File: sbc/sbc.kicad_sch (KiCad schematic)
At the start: 15 parts, among them U1 Sally, U2 Antic, U3 GTIA, U4 Pokey, U5 PIA, U6 74AHCT1G125GV,125, U7 74AHCT1G125GV,125, X1 3.579545 MHz

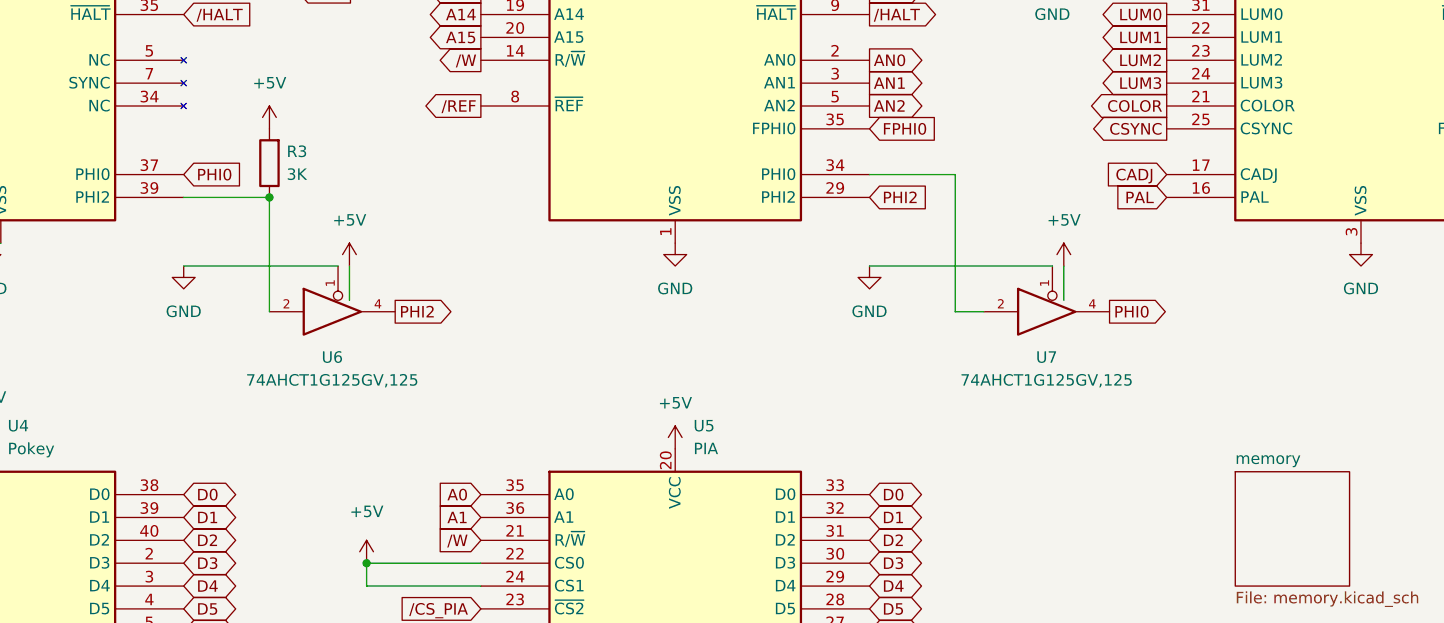
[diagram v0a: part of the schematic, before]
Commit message: SBC v1.1
PCB fixes/changes:

  - Permanently power voltage translators
  - Conservatively specified a slower SRAM (the previous/faster SRAM does actually work fine)
  - RMU: Speculatively provided unbuffered PHI0 input and OE output (not actually needed)
  - Add pullups to open drain GTIA outputs
  - Plot selected values on silk screen
  - Accommodate KiCad 7 upgrade

- PLD changes:
  - Fix AMU logic
  - Fix RMU (unbuffered PHI0 and OE output not needed)

- QTPY firmware:
  - add soft power on/off support (Ctrl-F12)
  - reflects switched power and usb state in the neopixel
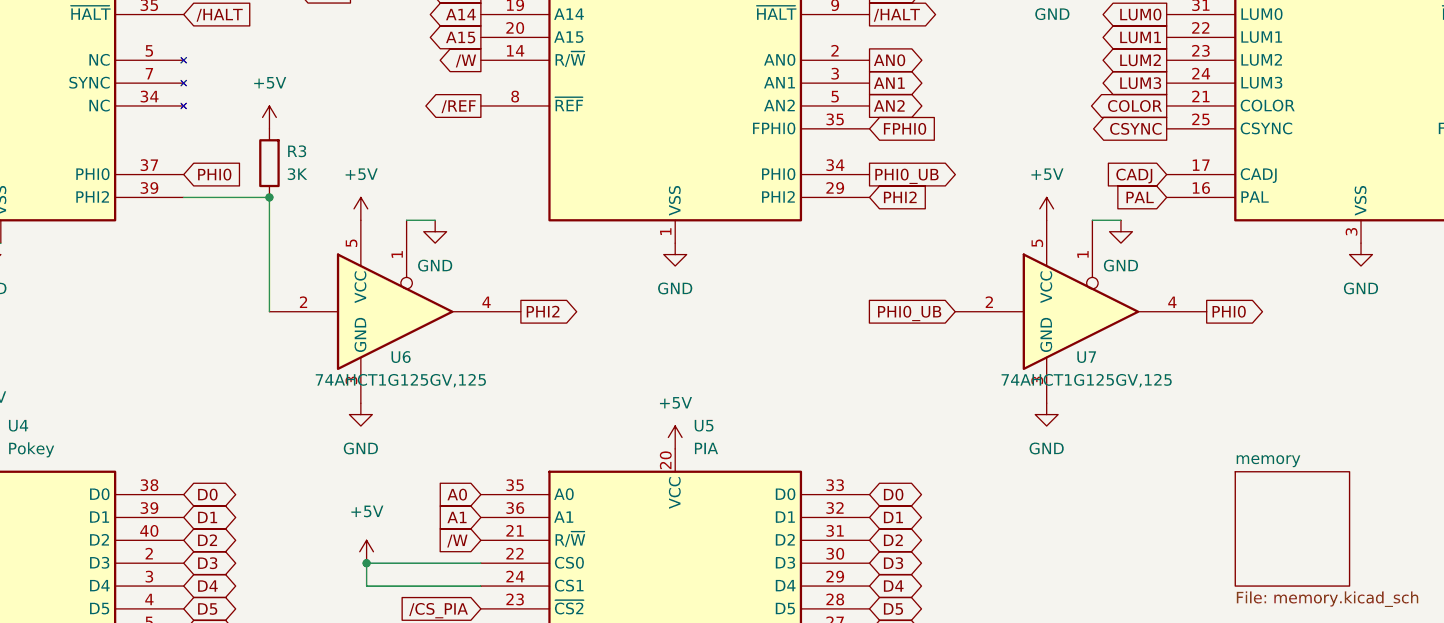
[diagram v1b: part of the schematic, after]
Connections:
- net PHI0_UB: now reaches U2.34 (PHI0), U7.2

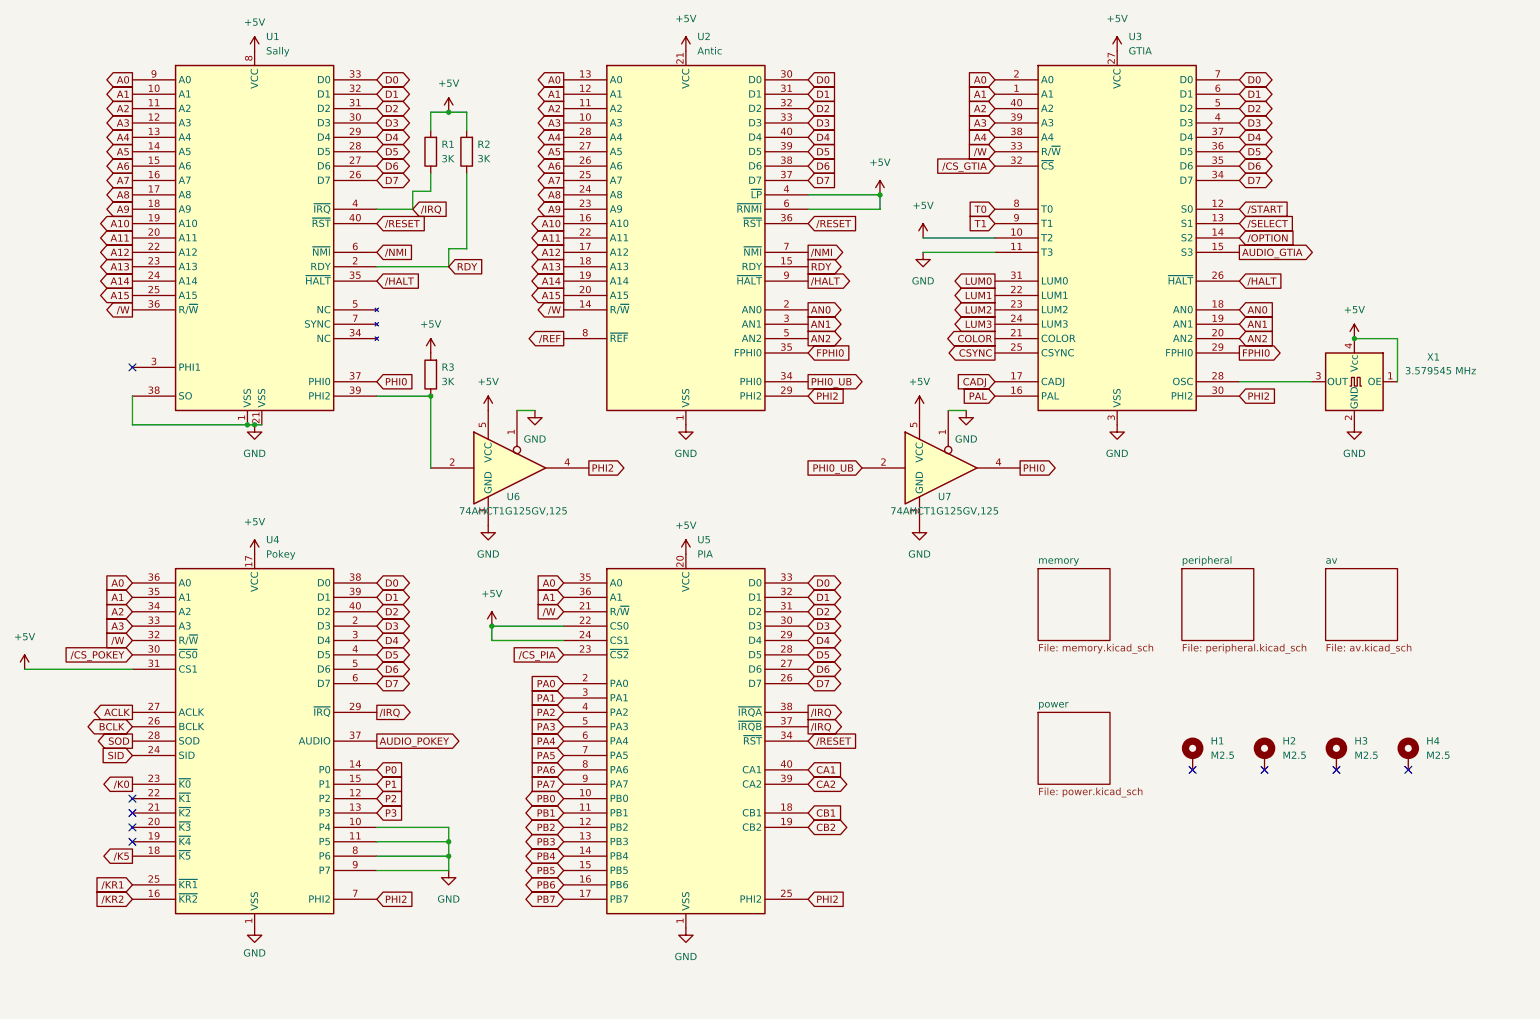
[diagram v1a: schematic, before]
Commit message: SBC v1.2
SBC fixes/changes:

  - S-Video:
    - Fix S-Video footprint (Y and C swapped, and GNDs swapped) and adapt schematic to match
    - Wire S-Video grounds to AVA header instead of directly to (digital) GND
  - Audio:
    - Wire Audio-Out ground to AVA header
    - Drop SIO audio
    - Pullup open drain pokey audio
  - AMU/RMU:
    - Connect ROM and RAM OE to GND
    - Reserve AMU pin for "IO"
    - Reserve RMU pin for "antic" (registered halt)
    - Support for separate Antic banking (clock RMU with /phi2)
    - Supoprt 130XE and 320XE (compy)
  - Add the option for a resistor between OSC, PHI0 buffer and PHI2 buffer (to reduce over/under-shoot)
  - Invert CA2 (a PNP transistor on the Atari 800 XL inverts this signal)

Additions:

  - SBC Audio/Video board
  - SBC Case
  - SBC SD board

Stylize the complete system as "SFF 320XE".
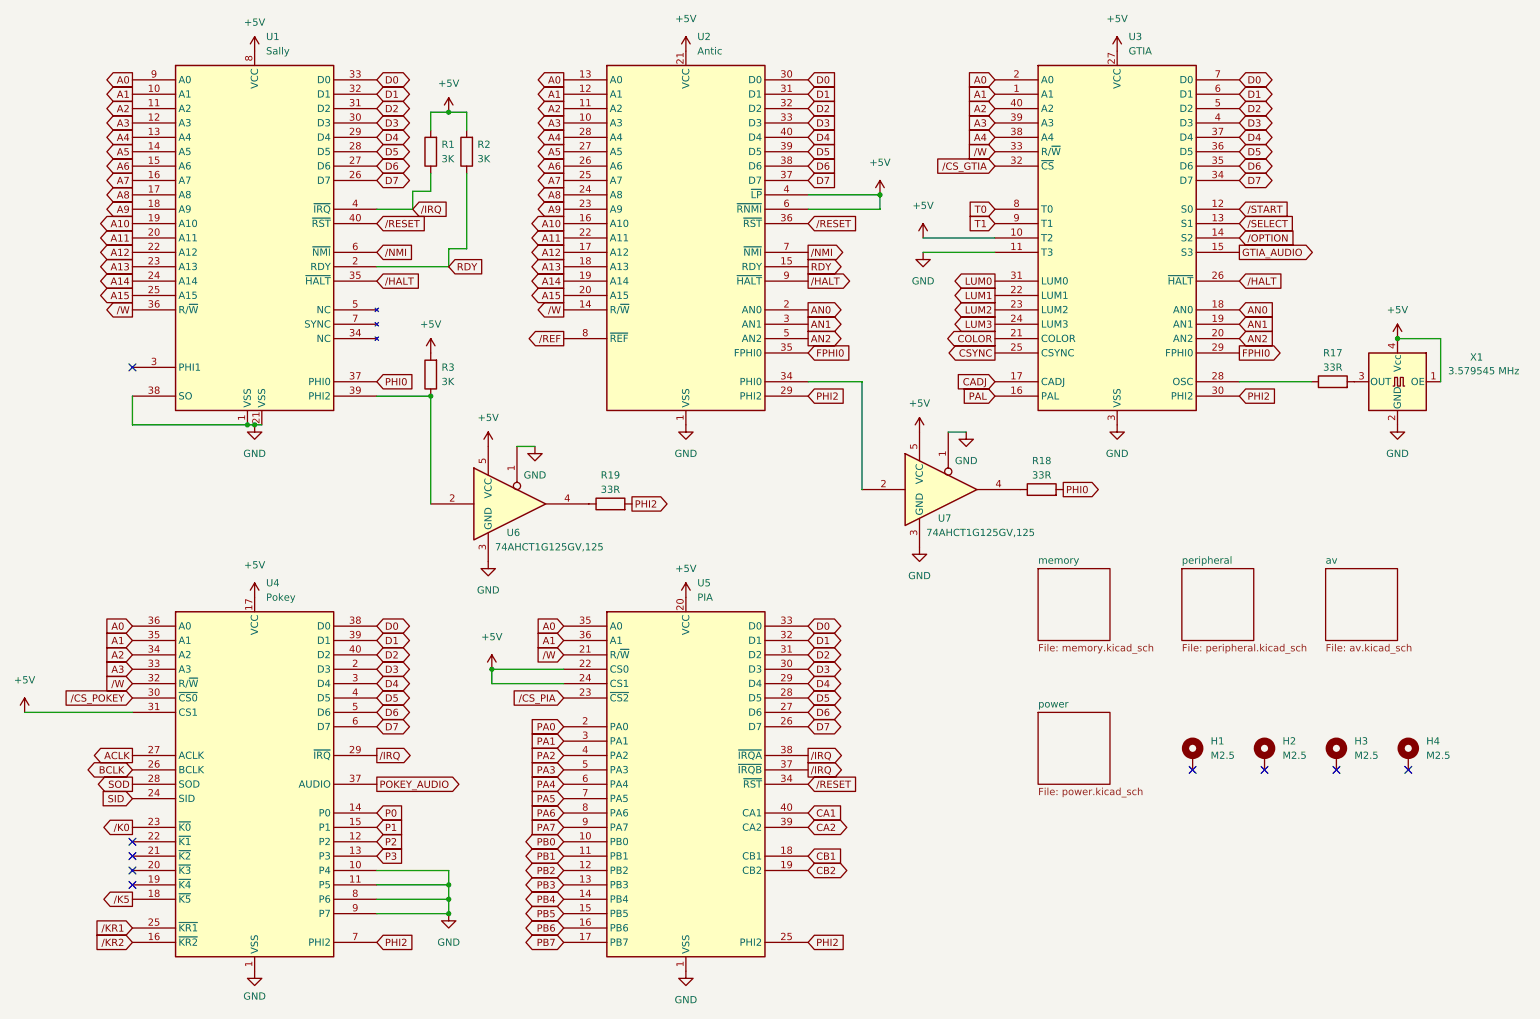
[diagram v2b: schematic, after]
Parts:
- added R17, R18, R19: 33R, Resistor_SMD:R_0805_2012Metric_Pad1.20x1.40mm_HandSolder, symbol Device:R
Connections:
- net PHI0: now also R18.2; no longer U7.4
- net PHI2: now also R19.2; no longer U6.4
- net at X1.3 (OUT): now also R17.2; no longer U3.28 (OSC)
- net AUDIO_GTIA renamed GTIA_AUDIO
- net AUDIO_POKEY renamed POKEY_AUDIO
- net PHI0_UB: no longer names the net of U2.34 (PHI0), U7.2
- new net: R19.1, U6.4
- new net: R18.1, U7.4
- new net: R17.1, U3.28 (OSC)
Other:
- moved on the sheet: U4, U5, U6, U7, X1

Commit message: SBC v1.3
Motherboard updates:

  - KiCad 9 upgrade
  - USB-C power connector
  - Replace EOL resistor packs with discrete SMD resistors
  - Power/enable voltage translators from switched 5V
  - Fix motor signal pullup
  - Eliminate loop in phi2 traces
  - Thicker clock signal traces

SD card adapter updates:

  - KiCad 9 upgrade
  - Power/enable voltage translator from switched 5V and the eliminate unnecessary SIO pullups

Audio/Video adapter updates:

  - KiCad 9 upgrade
  - No functional changes, gerbers not regenerated, cleaned up bom
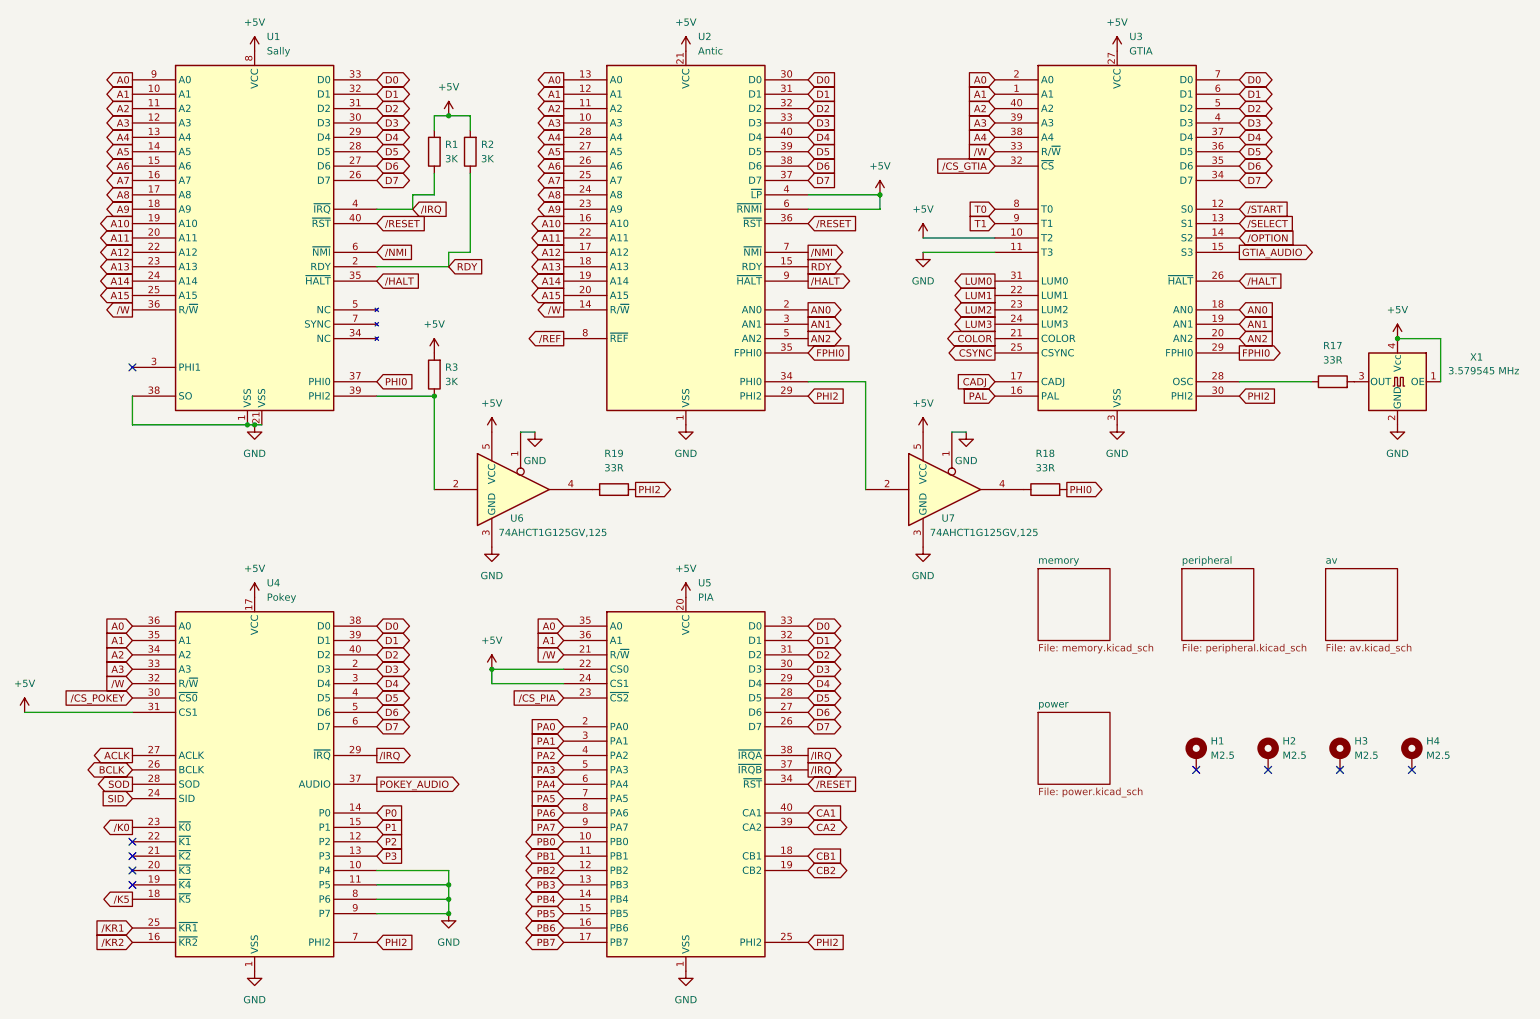
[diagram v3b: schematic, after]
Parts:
- H1, H2, H3, H4: now left out of the parts list
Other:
- moved on the sheet: H1, H2, H3, H4, R1, R18, R19, R2, R3, U6, U7
